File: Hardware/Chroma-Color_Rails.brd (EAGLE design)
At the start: 106.4 x 50.5 mm, 92 parts, among them J1 15-91-1102, J2 87832-6422, J3 1775470-6, J4 D2514-6V0C-AR-WD, J7 26-64-4040, U1 EP4CE6E22C8N, U2 ADP3338AKCZ-3.3-RL, U3 ADP3338AKCZ-2.5-RL, U4 NCV565ST12T3G, U5 M25P40-VMN6TPBCT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

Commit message: Added Fids. Working on Rail version.
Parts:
- moved C11 6.35 mm to (78.2, 42.2)
- moved C12 6.35 mm to (83.6, 42.2)
- moved C13 6.35 mm to (30.7, 22.4)
- moved C14 6.35 mm to (87.6, 40.4)
- moved C15 6.35 mm to (78.2, 40.4)
- moved C16 6.35 mm to (68.8, 42.2)
- moved C17 6.35 mm to (74.2, 42.2)
- moved C19 6.35 mm to (64.5, 40.4)
- moved C2 6.35 mm to (59.7, 28.7)
- moved C20 6.35 mm to (64.5, 42.2)
- moved C23 6.35 mm to (74.2, 40.4)
- moved C24 6.35 mm to (68.8, 40.4)
- moved C25 6.35 mm to (59.2, 24.4)
- moved C3 6.35 mm to (52.3, 38.4)
- moved C30 6.35 mm to (54.6, 38.4)
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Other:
- board size 106.4 x 50.5 mm -> 106.4 x 63.2 mm

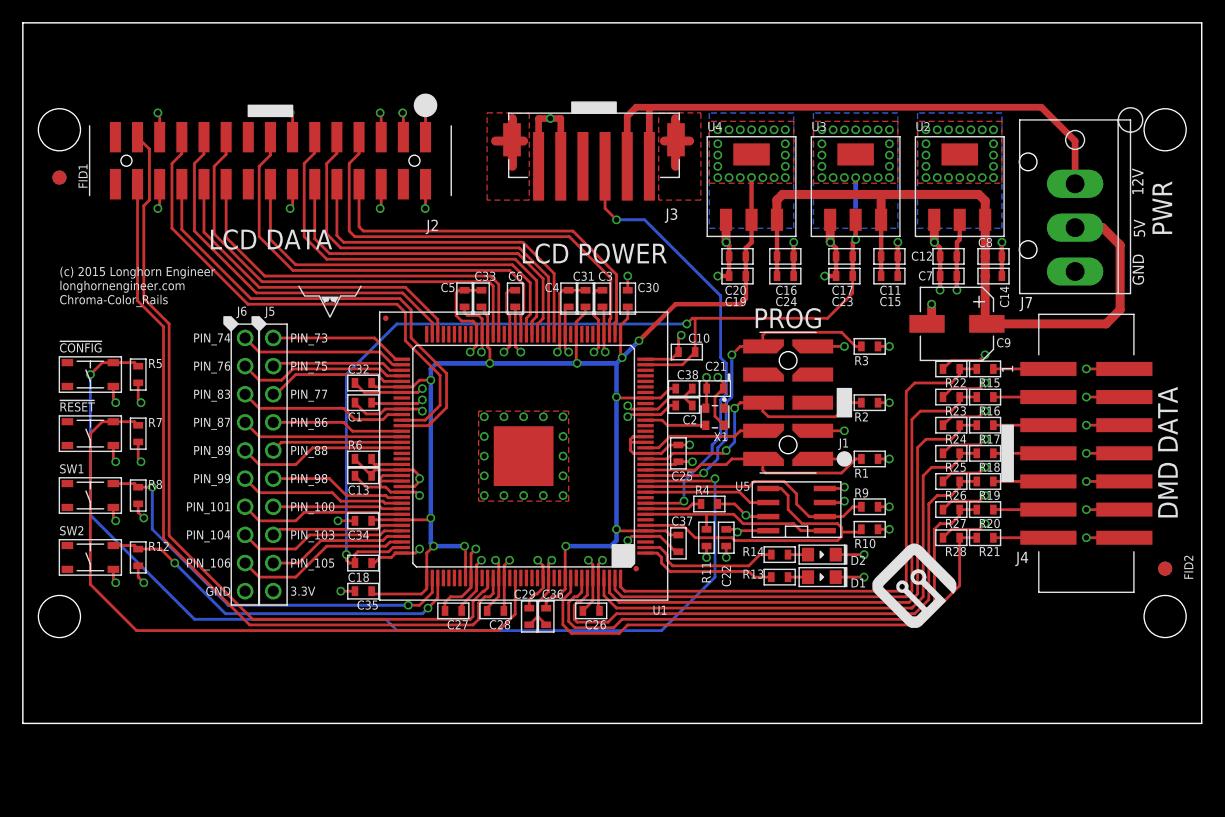
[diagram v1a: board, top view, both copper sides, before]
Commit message: Rev2 start. Fixed JTAG programming cable.
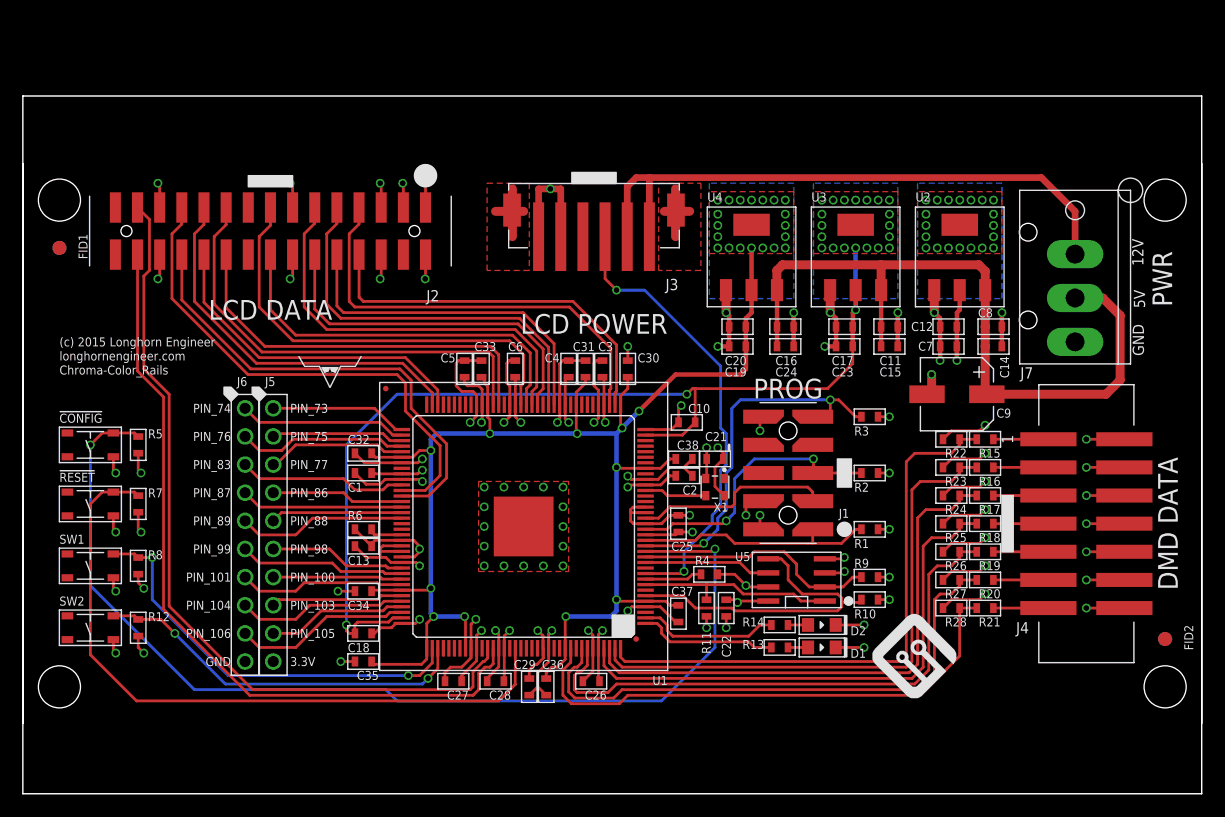
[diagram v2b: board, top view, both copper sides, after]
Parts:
- moved C11 6.35 mm to (78.2, 35.8)
- moved C12 6.35 mm to (83.6, 35.8)
- moved C13 6.35 mm to (30.7, 16.0)
- moved C14 6.35 mm to (87.6, 34.0)
- moved C15 6.35 mm to (78.2, 34.0)
- moved C16 6.35 mm to (68.8, 35.8)
- moved C17 6.35 mm to (74.2, 35.8)
- moved C19 6.35 mm to (64.5, 34.0)
- moved C2 6.35 mm to (59.7, 22.4)
- moved C20 6.35 mm to (64.5, 35.8)
- moved C23 6.35 mm to (74.2, 34.0)
- moved C24 6.35 mm to (68.8, 34.0)
- moved C25 6.35 mm to (59.2, 18.0)
- moved C3 6.35 mm to (52.3, 32.0)
- moved C30 6.35 mm to (54.6, 32.0)
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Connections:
- net 3.3V: now also J1.4; no longer J1.3
- net GND: now also J1.10, J1.2; no longer J1.1, J1.9
- net TCK: now also J1.1; no longer J1.2
- net TDI: now also J1.9; no longer J1.10
- net TDO: now also J1.3; no longer J1.4
- net TMS: now also J1.5; no longer J1.6
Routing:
- net TDO: track 11.3 -> 17.9 mm
- net GND: track 273.3 -> 268.9 mm
- net TDI: track 30.9 -> 34.5 mm
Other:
- board size 106.4 x 63.2 mm -> 106.4 x 63 mm
